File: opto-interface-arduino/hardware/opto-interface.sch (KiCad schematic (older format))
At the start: 11 parts, among them P1 CONN_02X06, U1 LM7805, U2 LM7905

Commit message: Add library papers and do initial Arduino Shield board layout.
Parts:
- added D1: ZENER, TO_SOT_Packages_SMD:SOT-23, symbol ZENER
- added R3: 1k3R, Resistors_SMD:R_0805_HandSoldering, symbol R
- renumbered R3 to R4
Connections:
- net labels added: +3V3
- wire segments 39 -> 47
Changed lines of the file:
@@
 $EndComp
 $Comp
-L R R3
+L R R4
 U 1 1 56A61D1F
 P 6600 3150
-F 0 "R3" H 6670 3196 50  0000 L CNN
+F 0 "R4" H 6670 3196 50  0000 L CNN
 F 1 "390R" H 6670 3104 50  0000 L CNN
 F 2 "Resistors_SMD:R_0805_HandSoldering" V 6530 3150 50  0001 C CNN
@@
 $EndComp
 $Comp
-L -12V #PWR7
+L -12V #PWR10
 U 1 1 56A63F07
 P 8200 3000
-F 0 "#PWR7" H 8200 3100 50  0001 C CNN
+F 0 "#PWR10" H 8200 3100 50  0001 C CNN
 F 1 "-12V" V 8218 3127 50  0000 L CNN
 F 2 "" H 8200 3000 50  0000 C CNN
@@
 Connection ~ 9900 2100
 $Comp
-L -5V #PWR11
+L -5V #PWR14
 U 1 1 56A640D9
 P 10300 3000
-F 0 "#PWR11" H 10300 3100 50  0001 C CNN
+F 0 "#PWR14" H 10300 3100 50  0001 C CNN
 F 1 "-5V" V 10318 3128 50  0000 L CNN
 F 2 "" H 10300 3000 50  0000 C CNN
@@
 $EndComp
 Connection ~ 9900 3000
+$Comp
+L ZENER D1
+U 1 1 56A89EF2
+P 6400 1700
+F 0 "D1" V 6354 1779 50  0000 L CNN
+F 1 "ZENER" V 6446 1779 50  0000 L CNN
+F 2 "TO_SOT_Packages_SMD:SOT-23" H 6400 1700 50  0001 C CNN
+F 3 "" H 6400 1700 50  0000 C CNN
+	1    6400 1700
+	0    1    1    0
+$EndComp
+$Comp
+L GND #PWR09
+U 1 1 56A8A09D
+P 6400 2200
+F 0 "#PWR09" H 6400 1950 50  0001 C CNN
+F 1 "GND" H 6408 2026 50  0000 C CNN
+F 2 "" H 6400 2200 50  0000 C CNN
+F 3 "" H 6400 2200 50  0000 C CNN
+	1    6400 2200
+	1    0    0    -1
+$EndComp
+Wire Wire Line
+	6400 1500 6400 1200
+Wire Wire Line
+	6400 2200 6400 1900
+Wire Wire Line
+	5900 1800 6100 1800
+Wire Wire Line
+	6100 1800 6100 1400
+Wire Wire Line
+	6100 1400 6400 1400
+Connection ~ 6400 1400
+$Comp
+L R R3
+U 1 1 56A8A23F
+P 6400 1050
+F 0 "R3" H 6470 1096 50  0000 L CNN
+F 1 "1k3R" H 6470 1004 50  0000 L CNN
+F 2 "Resistors_SMD:R_0805_HandSoldering" V 6330 1050 50  0001 C CNN
+F 3 "" H 6400 1050 50  0000 C CNN
+	1    6400 1050
+	1    0    0    -1
+$EndComp
+$Comp
+L +3V3 #PWR010
+U 1 1 56A8A5AE
+P 3800 2000
+F 0 "#PWR010" H 3800 1850 50  0001 C CNN
+F 1 "+3V3" H 3818 2174 50  0000 C CNN
+F 2 "" H 3800 2000 50  0000 C CNN
+F 3 "" H 3800 2000 50  0000 C CNN
+	1    3800 2000
+	1    0    0    -1
+$EndComp
+Wire Wire Line
+	3800 2000 3800 2300
+Wire Wire Line
+	3800 2300 4000 2300
+$Comp
+L +3V3 #PWR011
+U 1 1 56A8A646
+P 6400 700
+F 0 "#PWR011" H 6400 550 50  0001 C CNN
+F 1 "+3V3" H 6418 874 50  0000 C CNN
+F 2 "" H 6400 700 50  0000 C CNN
+F 3 "" H 6400 700 50  0000 C CNN
+	1    6400 700
+	1    0    0    -1
+$EndComp
+Wire Wire Line
+	6400 700  6400 900
 $EndSCHEMATC

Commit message: Update to include external power connector.
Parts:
- added P2: CONN_01X06, Pin_Headers:Pin_Header_Straight_1x06, symbol CONN_01X06
- C1, C2: symbol C -> C-RESCUE-opto-interface
- C3, C4: symbol CP -> CP-RESCUE-opto-interface
- D1: symbol ZENER -> ZENER-RESCUE-opto-interface
- R1, R2, R3, R4: symbol R -> R-RESCUE-opto-interface
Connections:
- wire segments 47 -> 54
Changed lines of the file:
@@
 EESchema Schematic File Version 2
+LIBS:opto-interface-rescue
 LIBS:power
 LIBS:device
@@
 LIBS:valves
 LIBS:arduino_shieldsNCL
+LIBS:borniers
 LIBS:opto-interface-cache
 EELAYER 25 0
@@
 $EndComp
 $Comp
-L R R4
+L R-RESCUE-opto-interface R4
 U 1 1 56A61D1F
 P 6600 3150
@@
 $EndComp
 $Comp
-L R R2
+L R-RESCUE-opto-interface R2
 U 1 1 56A61E09
 P 3300 3850
@@
 $EndComp
 $Comp
-L R R1
+L R-RESCUE-opto-interface R1
 U 1 1 56A61E93
 P 2800 3850
@@
 	9700 1600 10100 1600
 $Comp
-L C C1
+L C-RESCUE-opto-interface C1
 U 1 1 56A63A9E
 P 8600 1950
@@
 Connection ~ 9300 2100
 $Comp
-L CP C3
+L CP-RESCUE-opto-interface C3
 U 1 1 56A63B52
 P 9900 1850
@@
 $EndComp
 $Comp
-L C C2
+L C-RESCUE-opto-interface C2
 U 1 1 56A63DBB
 P 8600 2650
@@
 $EndComp
 $Comp
-L CP C4
+L CP-RESCUE-opto-interface C4
 U 1 1 56A63E65
 P 9900 2650
@@
 $EndComp
 $Comp
-L -12V #PWR10
+L -12V #PWR15
 U 1 1 56A63F07
 P 8200 3000
-F 0 "#PWR10" H 8200 3100 50  0001 C CNN
+F 0 "#PWR15" H 8200 3100 50  0001 C CNN
 F 1 "-12V" V 8218 3127 50  0000 L CNN
 F 2 "" H 8200 3000 50  0000 C CNN
@@
 Connection ~ 9900 2100
 $Comp
-L -5V #PWR14
+L -5V #PWR19
 U 1 1 56A640D9
 P 10300 3000
-F 0 "#PWR14" H 10300 3100 50  0001 C CNN
+F 0 "#PWR19" H 10300 3100 50  0001 C CNN
 F 1 "-5V" V 10318 3128 50  0000 L CNN
 F 2 "" H 10300 3000 50  0000 C CNN
@@
 Connection ~ 9900 3000
 $Comp
-L ZENER D1
+L ZENER-RESCUE-opto-interface D1
 U 1 1 56A89EF2
 P 6400 1700
@@
 Connection ~ 6400 1400
 $Comp
-L R R3
+L R-RESCUE-opto-interface R3
 U 1 1 56A8A23F
 P 6400 1050
@@
 Wire Wire Line
 	6400 700  6400 900
+$Comp
+L CONN_01X06 P2
+U 1 1 56B5E697
+P 7250 3700
+F 0 "P2" V 7215 3356 50  0000 R CNN
+F 1 "CONN_01X06" V 7123 3356 50  0000 R CNN
+F 2 "Pin_Headers:Pin_Header_Straight_1x06" H 7250 3700 60  0001 C CNN
+F 3 "" H 7250 3700 60  0000 C CNN
+	1    7250 3700
+	0    -1   -1   0
+$EndComp
+$Comp
+L +12V #PWR012
+U 1 1 56B5E738
+P 7000 4300
+F 0 "#PWR012" H 7000 4150 60  0001 C CNN
+F 1 "+12V" H 7018 4481 60  0000 C CNN
+F 2 "" H 7000 4300 60  0000 C CNN
+F 3 "" H 7000 4300 60  0000 C CNN
+	1    7000 4300
+	-1   0    0    1
+$EndComp
+$Comp
+L +5V #PWR013
+U 1 1 56B5E792
+P 7200 4300
+F 0 "#PWR013" H 7200 4150 60  0001 C CNN
+F 1 "+5V" H 7218 4481 60  0000 C CNN
+F 2 "" H 7200 4300 60  0000 C CNN
+F 3 "" H 7200 4300 60  0000 C CNN
+	1    7200 4300
+	-1   0    0    1
+$EndComp
+$Comp
+L -12V #PWR11
+U 1 1 56B5E808
+P 7100 4300
+F 0 "#PWR11" H 7100 4400 20  0001 C CNN
+F 1 "-12V" H 7102 4480 60  0000 C CNN
+F 2 "" H 7100 4300 60  0000 C CNN
+F 3 "" H 7100 4300 60  0000 C CNN
+	1    7100 4300
+	-1   0    0    1
+$EndComp
+$Comp
+L -5V #PWR13
+U 1 1 56B5E862
+P 7300 4300
+F 0 "#PWR13" H 7300 4400 20  0001 C CNN
+F 1 "-5V" H 7302 4480 60  0000 C CNN
+F 2 "" H 7300 4300 60  0000 C CNN
+F 3 "" H 7300 4300 60  0000 C CNN
+	1    7300 4300
+	-1   0    0    1
+$EndComp
+$Comp
+L GND #PWR014
+U 1 1 56B5E8BC
+P 7500 4300
+F 0 "#PWR014" H 7500 4050 60  0001 C CNN
+F 1 "GND" H 7508 4119 60  0000 C CNN
+F 2 "" H 7500 4300 60  0000 C CNN
+F 3 "" H 7500 4300 60  0000 C CNN
+	1    7500 4300
+	1    0    0    -1
+$EndComp
+Wire Wire Line
+	7000 3900 7000 4300
+Wire Wire Line
+	7100 3900 7100 4300
+Wire Wire Line
+	7200 3900 7200 4300
+Wire Wire Line
+	7300 3900 7300 4300
+Wire Wire Line
+	7400 3900 7400 4300
+Wire Wire Line
+	7400 4300 7500 4300
+Wire Wire Line
+	7500 4300 7500 3900
 $EndSCHEMATC

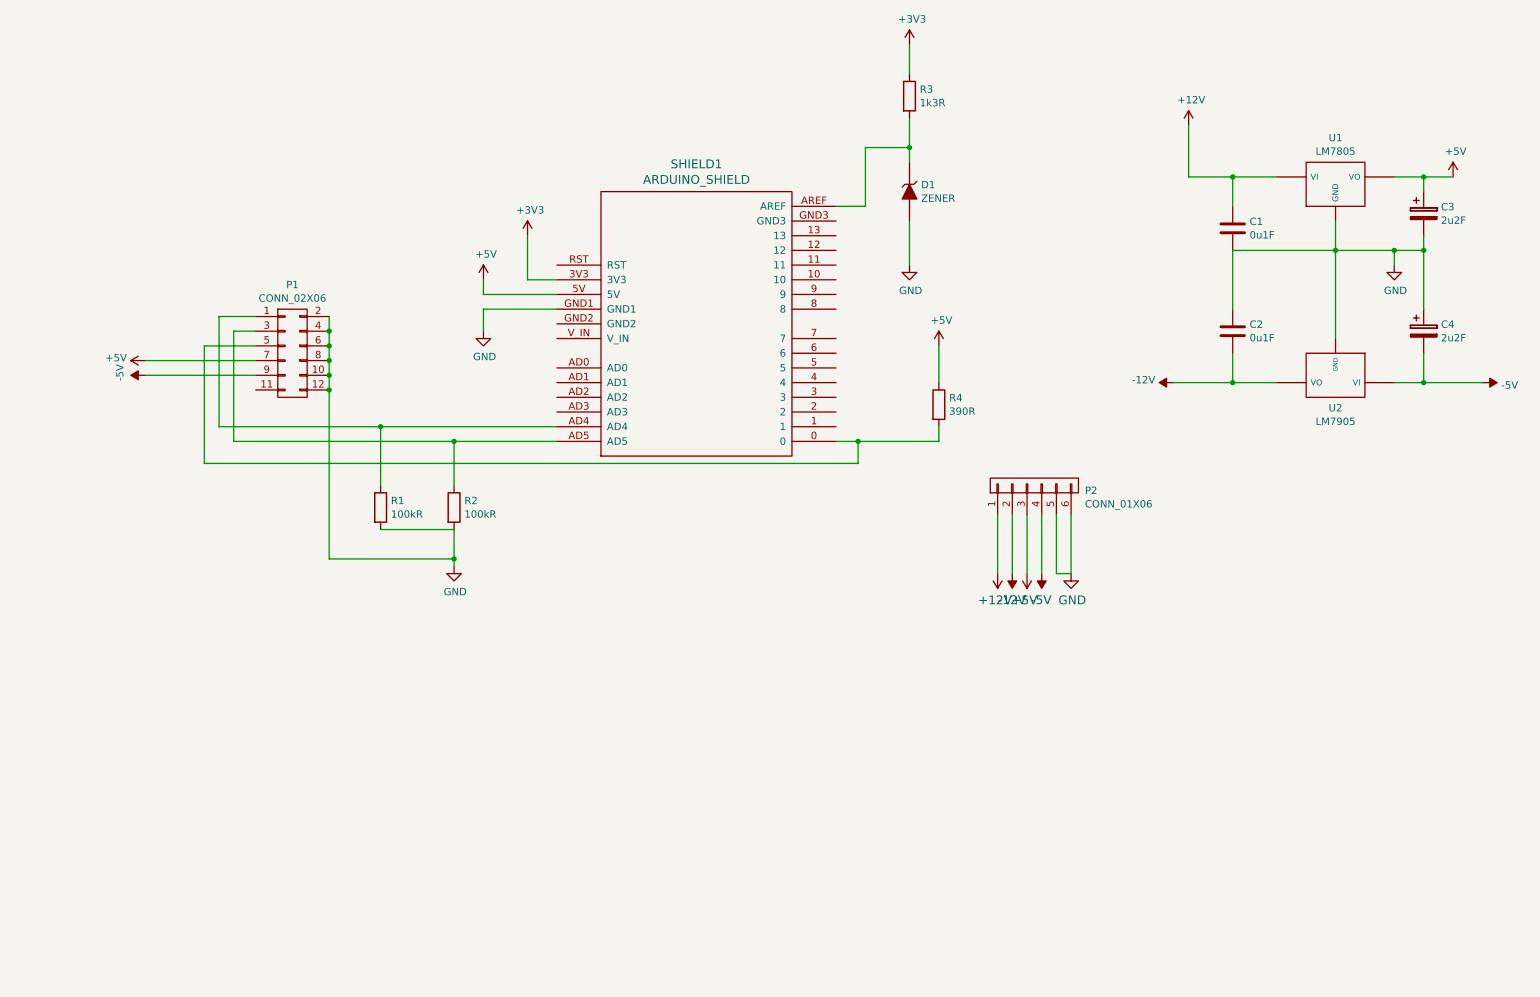
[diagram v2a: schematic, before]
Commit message: Add charge pump for -ve supply and skeleton input filter.  Add calculations document.
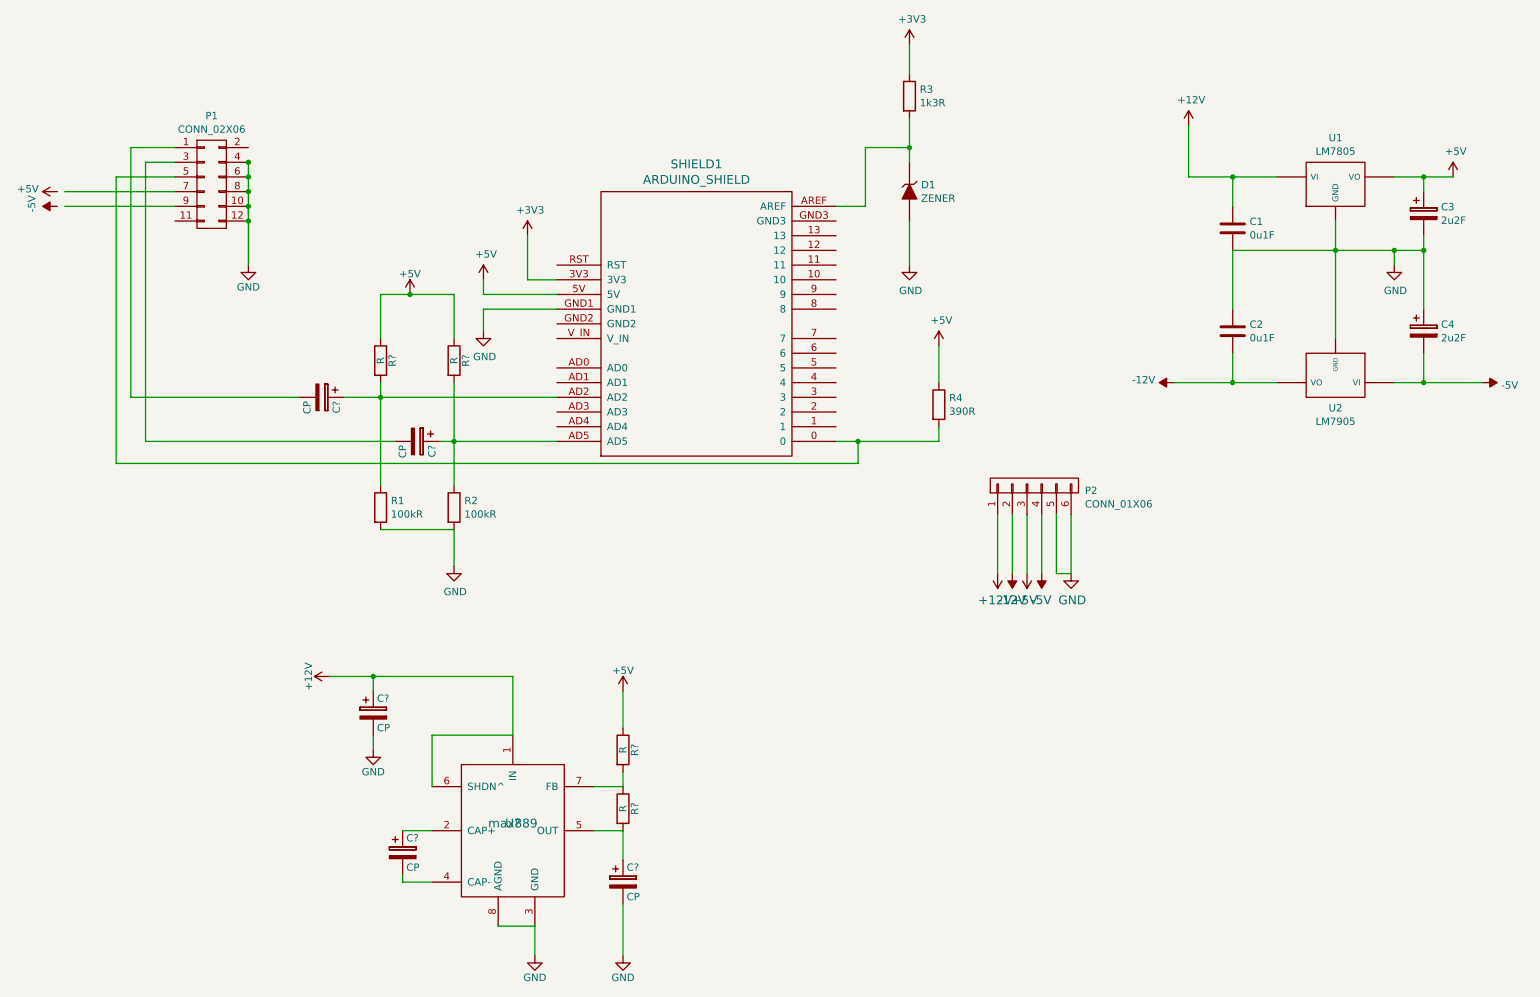
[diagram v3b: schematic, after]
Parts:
- added C? (x5): CP, symbol CP
- added R? (x4): R, symbol R
- added U?: max889, symbol max889
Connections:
- wire segments 54 -> 76
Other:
- moved on the sheet: P1
